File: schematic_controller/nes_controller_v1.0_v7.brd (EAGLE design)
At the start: 110.2 x 55.9 mm, 38 parts

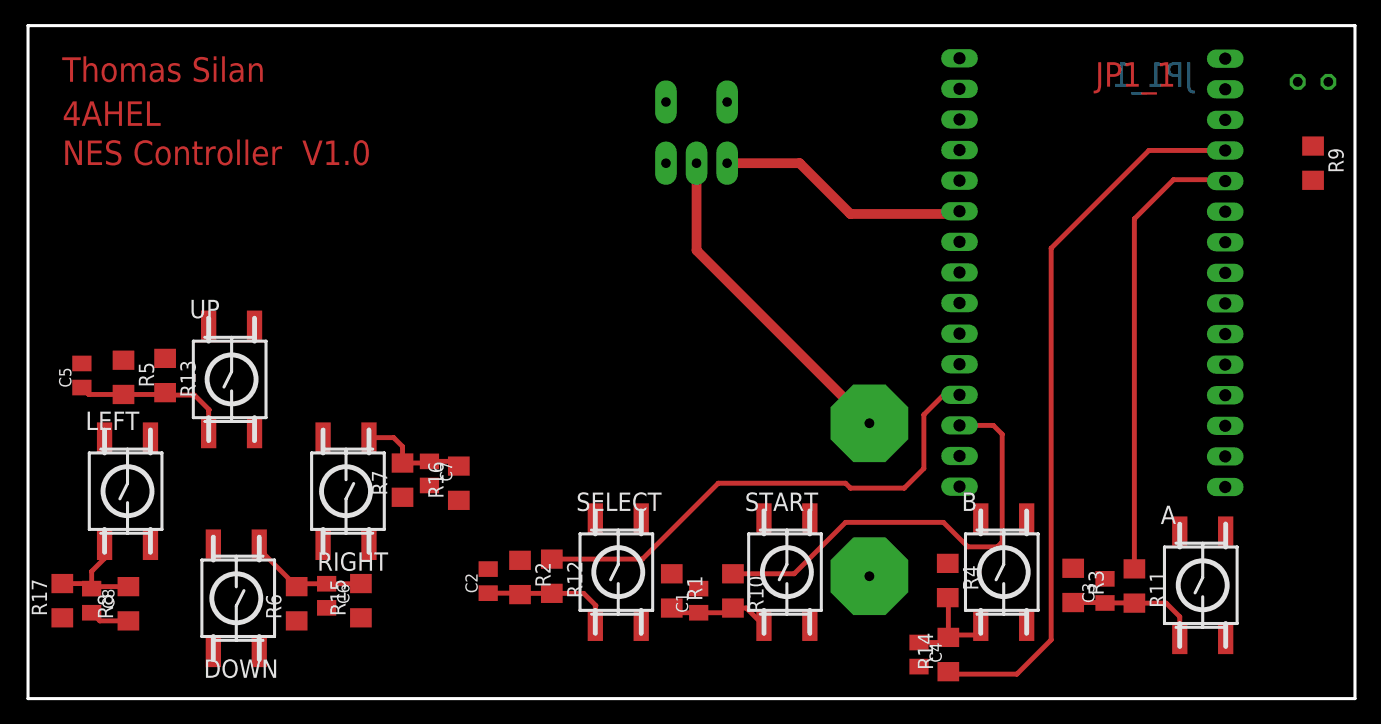
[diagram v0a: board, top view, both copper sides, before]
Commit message: changed bigger led hole
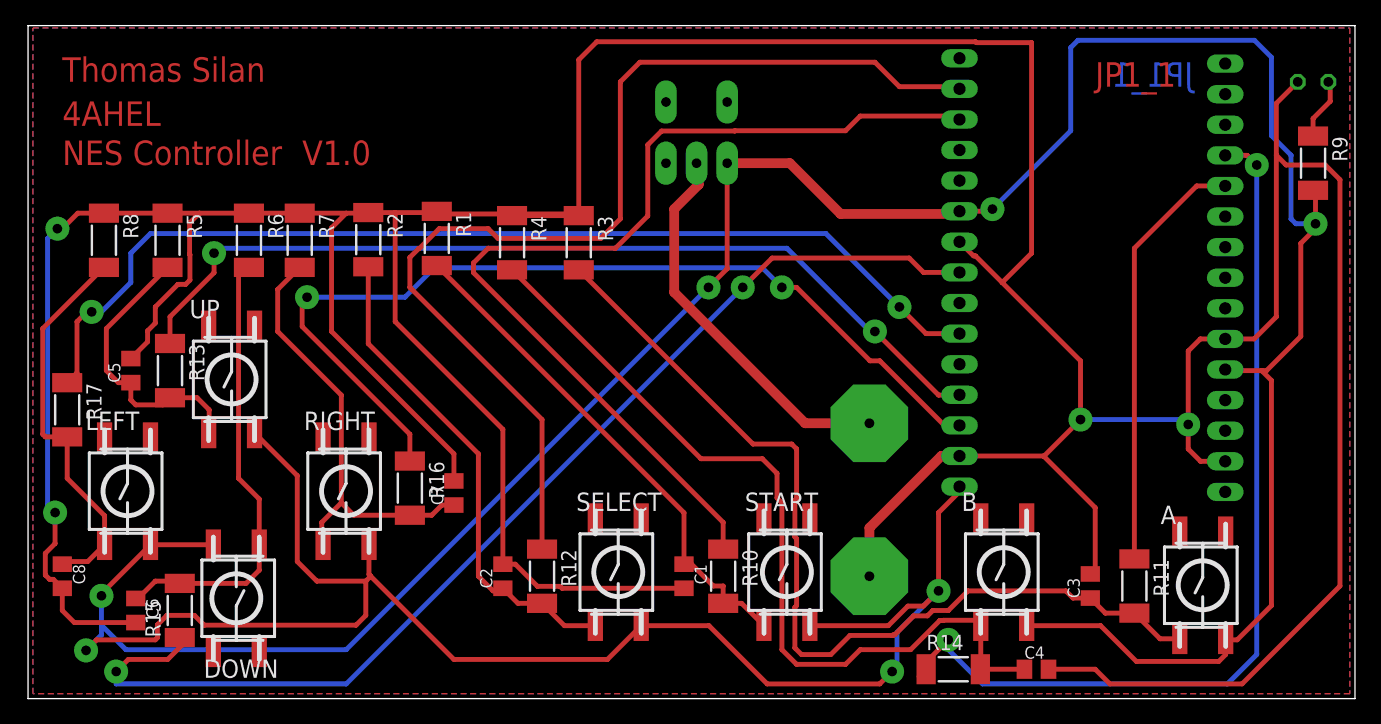
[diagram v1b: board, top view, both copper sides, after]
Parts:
- C1, C2, C3, C4, C5, C6, C7, C8: device rcl:C0805K -> rcl@1:C0805K
- R1, R10, R11, R12, R13, R14, R15, R16, R17, R2, R3, R4, R5, R6, R7, R8, R9: device rcl:R1206 -> rcl:MINI_MELF-0207R
- moved R3 49.9 mm to (45.7, 37.8)
- moved R4 45.8 mm to (40.2, 37.8)
- moved R1 35.2 mm to (33.9, 38.2)
- moved R2 30.7 mm to (28.2, 38.1)
- moved R6 30.4 mm to (18.3, 38.0), turned to 270 degrees
- moved R8 30.2 mm to (6.30, 38.0), turned to 270 degrees
- moved R7 21.7 mm to (22.6, 38.0), turned to 270 degrees
- moved C6 15.9 mm to (8.94, 7.32)
- moved R17 15.9 mm to (3.25, 24.0), turned to 270 degrees
- moved R15 15.1 mm to (12.6, 7.32)
- moved R5 12.0 mm to (11.6, 38.0)
- moved C4 9.83 mm to (83.7, 2.44), turned to 0 degrees
- moved C5 4.08 mm to (8.53, 27.2)
- moved R16 4.08 mm to (31.7, 17.5), turned to 270 degrees
- moved C8 3.17 mm to (2.84, 10.2)
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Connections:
- net N$4: no longer B.11
- net RIGHT: now also JP2.13; no longer JP2.3
- net SELECT: now also JP2.2; no longer JP2.12
- net START: now also JP2.3; no longer JP2.13
- net UP: now also JP2.12; no longer JP2.2
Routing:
- net GND: track 3.33 -> 425.5 mm, vias 0 -> 4
- net +3V3: track 21.1 -> 359.7 mm, vias 0 -> 7
- net DOWN: track 0.00 -> 94.0 mm, vias 0 -> 2
- net LEFT: track 0.00 -> 87.1 mm, vias 0 -> 2
- net RIGHT: track 0.00 -> 78.1 mm, vias 0 -> 2
- net UP: track 0.00 -> 76.4 mm, vias 0 -> 2
- net 4$5: track 11.2 -> 77.0 mm
- net N$4: track 9.34 -> 69.8 mm
- net SELECT: track 42.4 -> 89.4 mm
- net START: track 37.9 -> 81.3 mm
- net N$3: track 8.58 -> 42.9 mm
- net 3§4: track 11.2 -> 41.1 mm
- net N$6: track 10.2 -> 38.0 mm
- net N$7: track 9.35 -> 36.8 mm
- net N$8: track 9.82 -> 32.5 mm
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- added copper zone on layer 1, net GND
- added copper zone on layer 16, net GND
